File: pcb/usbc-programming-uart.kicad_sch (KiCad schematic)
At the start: 24 parts, among them J6 HC-TYPE-C-16P-01A, Q5 MMBT2222A, Q6 MMBT2222A, SW1 RST, SW2 BOOT, U10 AMS1117-3.3, U11 CH334R, U9 CH340C, Y1 12MHz

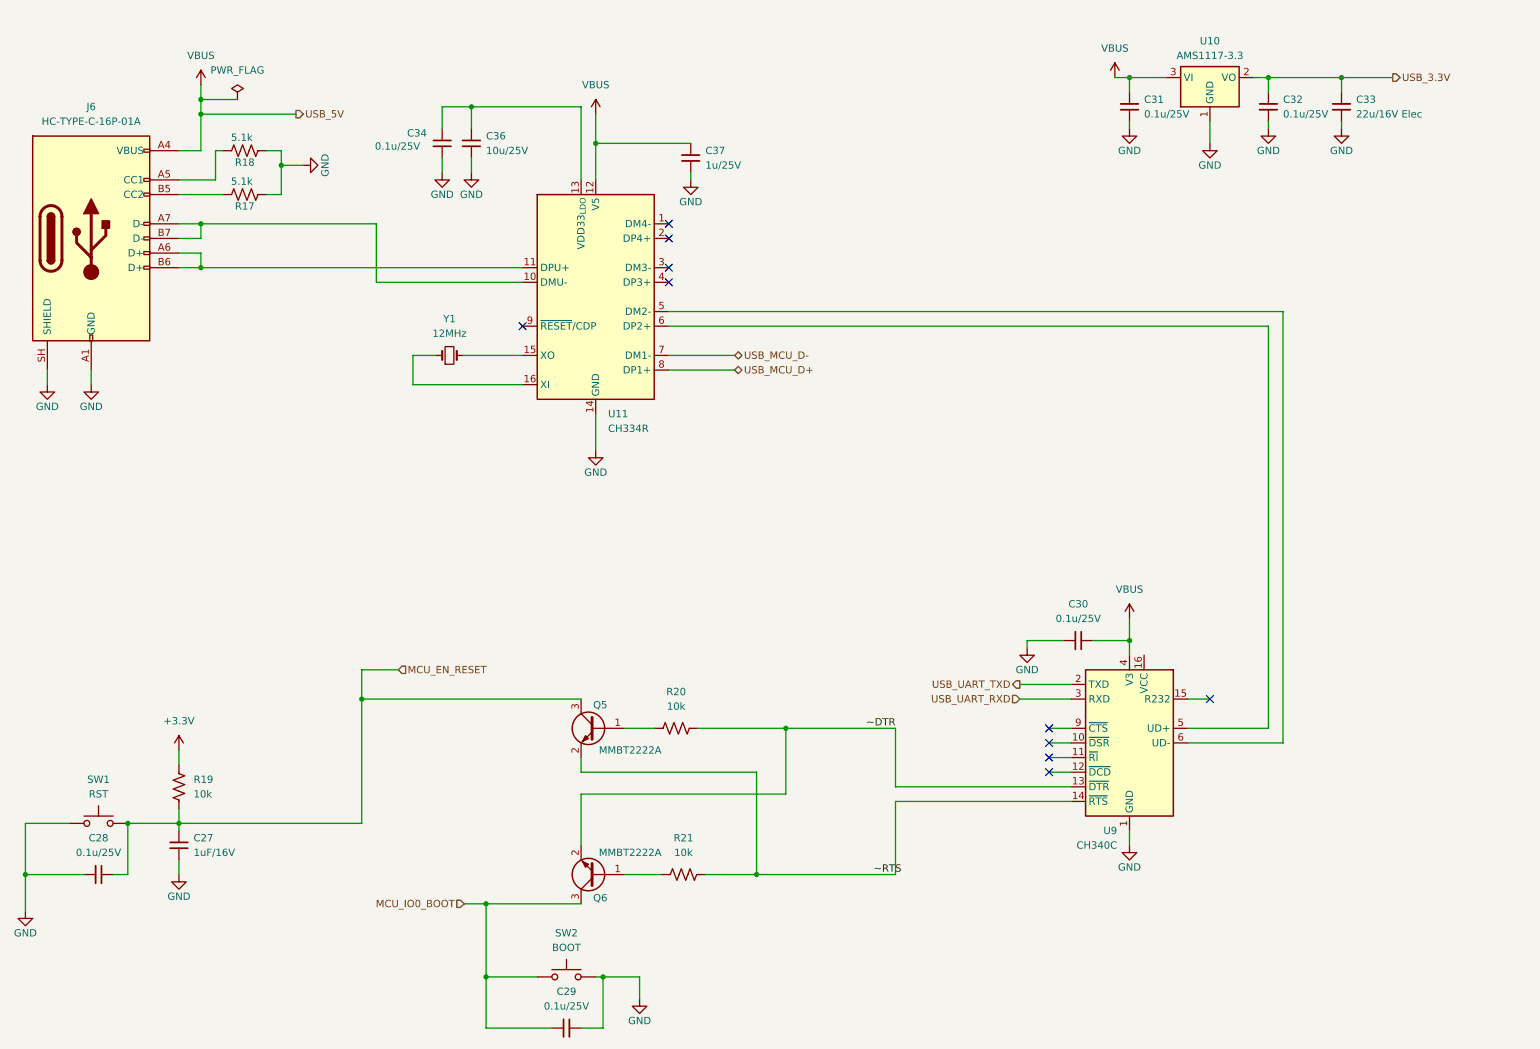
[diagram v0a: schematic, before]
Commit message: Replace battery/PowerPole ORing FETs with TPS2121 in VCOMP mode
power.kicad_sch: U12 (TPS2121RUXR) replaces the two LM74610+AO3400A ideal-
diode branches, configured per TI's "Highest Voltage Operation" (VCOMP,
Fig 10-15): PR1/CP2 tied to GND, OV1/OV2 resistor dividers (23.7k/5k) off
IN1 (PWR_18650) and IN2 (PWR_POWERPOLE), ILM set via R24 (51.1k), SS
ramped through C39 (0.01uF), ST tied directly to GND (unused). Divider
topology, ILM, and SS/ST wiring were each wrong on the first pass and
have been traced pin-by-pin and verified correct against the reference
schematic.

usbc-programming-uart.kicad_sch: CH340C VCC/V3 pin fix (VCC now correctly
powered from VBUS, V3 no longer driven externally) and F3 polyfuse
(16V/500mA) added in series on VBUS upstream of the hub/CH340/AMS1117.

battery_18650_input.kicad_sch, foxhunt1.kicad_pro: incidental KiCad
save cleanup (unused symbol-cache entry pruned, two collinear wire
segments merged, designator bookkeeping reordered) -- no circuit changes.

Bumps kicad_gx_library for the new TPS2121RUXR part. Adds
_docs/hardware/usb_battery_power_mux.md documenting the planned
3-stage TPS2121 architecture (this commit implements stage 1; stages
2/3, the USB-vs-regulator muxes, are not yet implemented).

Co-Authored-By: Claude Sonnet 5 <noreply@anthropic.com>
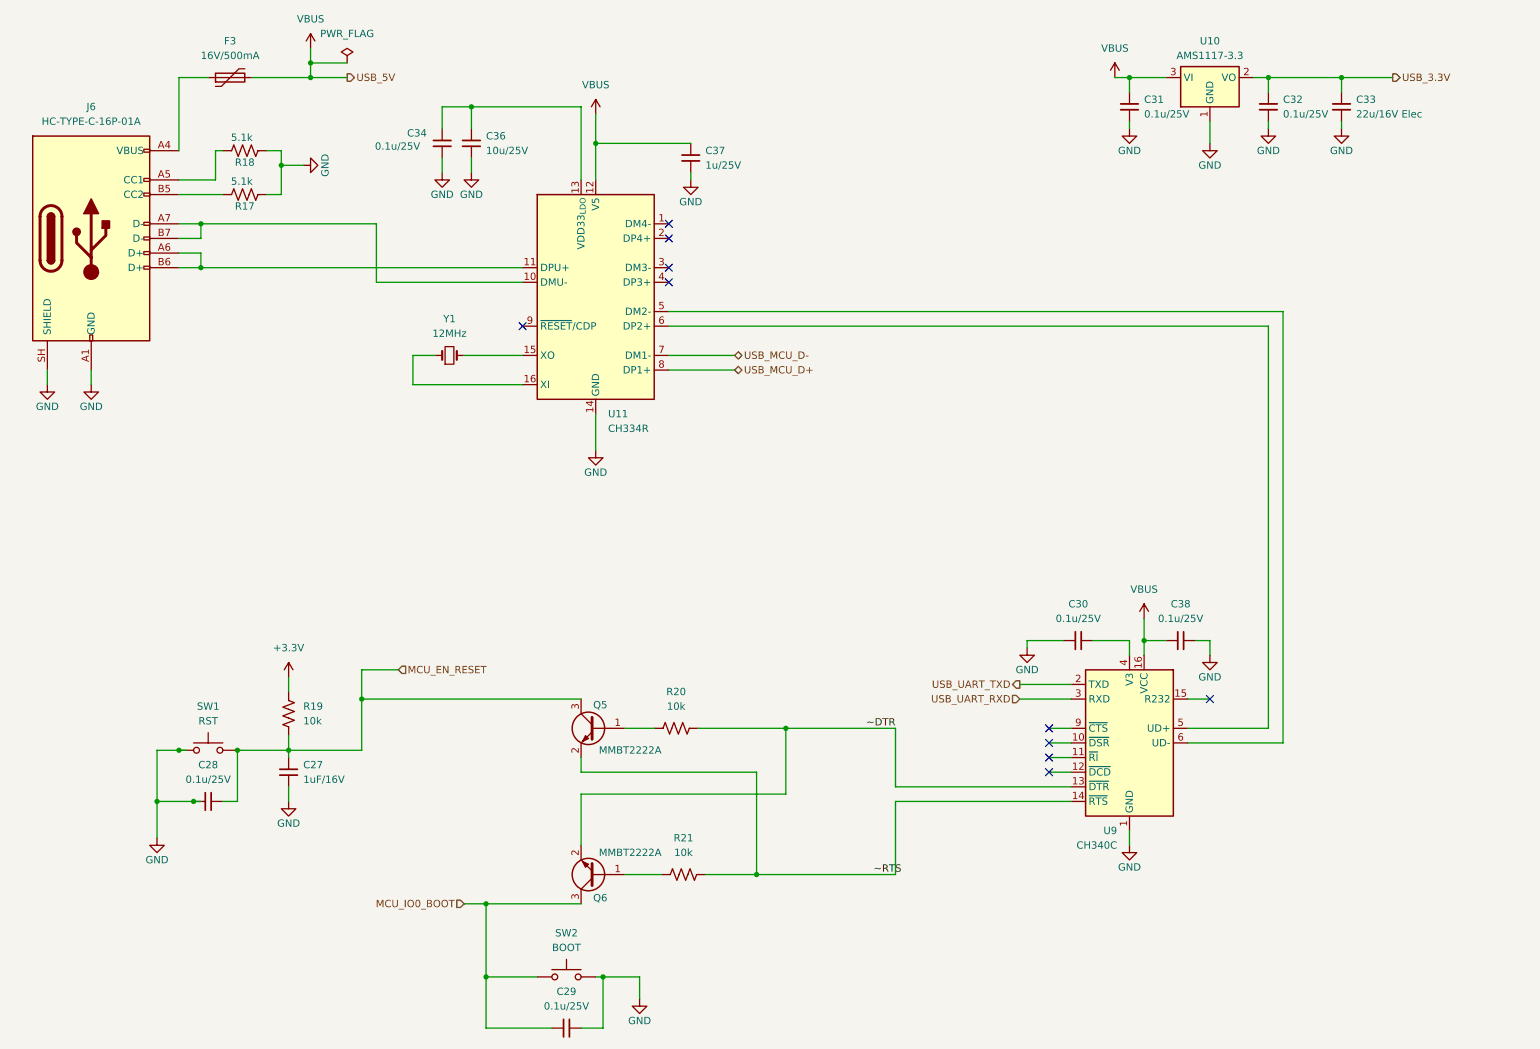
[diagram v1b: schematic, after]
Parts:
- added C38: 0.1u/25V, Capacitor_SMD:C_0603_1608Metric, symbol Device:C_Small
- added F3: 16V/500mA, Fuse:Fuse_0805_2012Metric, symbol Device:Polyfuse
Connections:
- net GND: now also C38.2
- net VBUS: now also U9.16 (VCC), C38.1, F3.2; no longer C30.2, J6.A4 (VBUS), J6.A9 (VBUS), J6.B4 (VBUS), J6.B9 (VBUS), U9.4 (V3)
- new net: F3.1, J6.A4 (VBUS), J6.A9 (VBUS), J6.B4 (VBUS), J6.B9 (VBUS)
- new net: C30.2, U9.4 (V3)
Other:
- moved on the sheet: C27, C28, R19, SW1

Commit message: Add TPS2121 Stage 2/3: USB-vs-battery priority muxing on 5V and 3.3V rails
power.kicad_sch:
- U14 (TPS2121RUXR): 5V rail mux. IN1=BATT_5V_REG (priority), IN2=USB_5V_IN,
  OUT=+5V. PR1 tied to IN1, CP2/OV1/OV2 to GND (VREF priority mode -- battery
  always wins when present, no voltage-comparison ambiguity between two
  nominally-5V sources). ILM set via R26 (30.1k, ~3.5A class, sized with
  margin above the 2A SA818 budget for TX current transients). SS via C42
  (0.01uF). ST feeds the battery/USB detect logic below.
- U13 (TPS2121RUXR): 3.3V rail mux, same configuration. IN1=BATT_3.3V_REG,
  IN2=USB_3.3V_IN, OUT=+3.3V. ILM via R25 (80.6k, ~1.5A class, vs 1A
  peripheral budget). SS via C41.
- U1 (74LVC1G08): AND-gates U13.ST and U14.ST (each pulled up individually
  via R27/R28, 10k to +3.3V, since ST is open-drain) into PWR_ON_BATTERY --
  high only when both rails are confirmed running from battery, low if
  either has fallen back to USB. Output exposed as a new Power sheet pin.

foxhunt1.kicad_sch: bridges PWR_ON_BATTERY (Power sheet) to the new
IO_IN_ON_BATT input on the mcu-esp32 sheet, and USB_3.3V_IN/USB_5V_IN
(Power sheet) to USB_3.3V/USB_5V (USB-C sheet) -- these were previously
unconnected placeholder labels.

mcu-esp32.kicad_sch: IO_IN_ON_BATT wired to U8 pin 35 (GPIO42), the one
GPIO the pinout doc had marked as still spare.

kicad_gx_library: TPS2121RUXR symbol fix (one OUT pin marked passive
instead of output, since the two physical OUT pins are meant to be tied
together -- avoids an ERC driver-conflict false positive).

power_regulation.kicad_sch, battery_18650_input.kicad_sch,
battery_powerpole_input.kicad_sch, foxhunt1.kicad_pro: incidental KiCad
save cleanup, no circuit changes (verified via orphan/short checks and
netlist diff -- same components as before).

Fully traced pin-by-pin: both mux dividers/ILM/SS wiring, the battery-vs-
USB source assignment on each rail (not swapped), the AND-gate inputs,
and all three cross-sheet bridges. 0 new orpha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
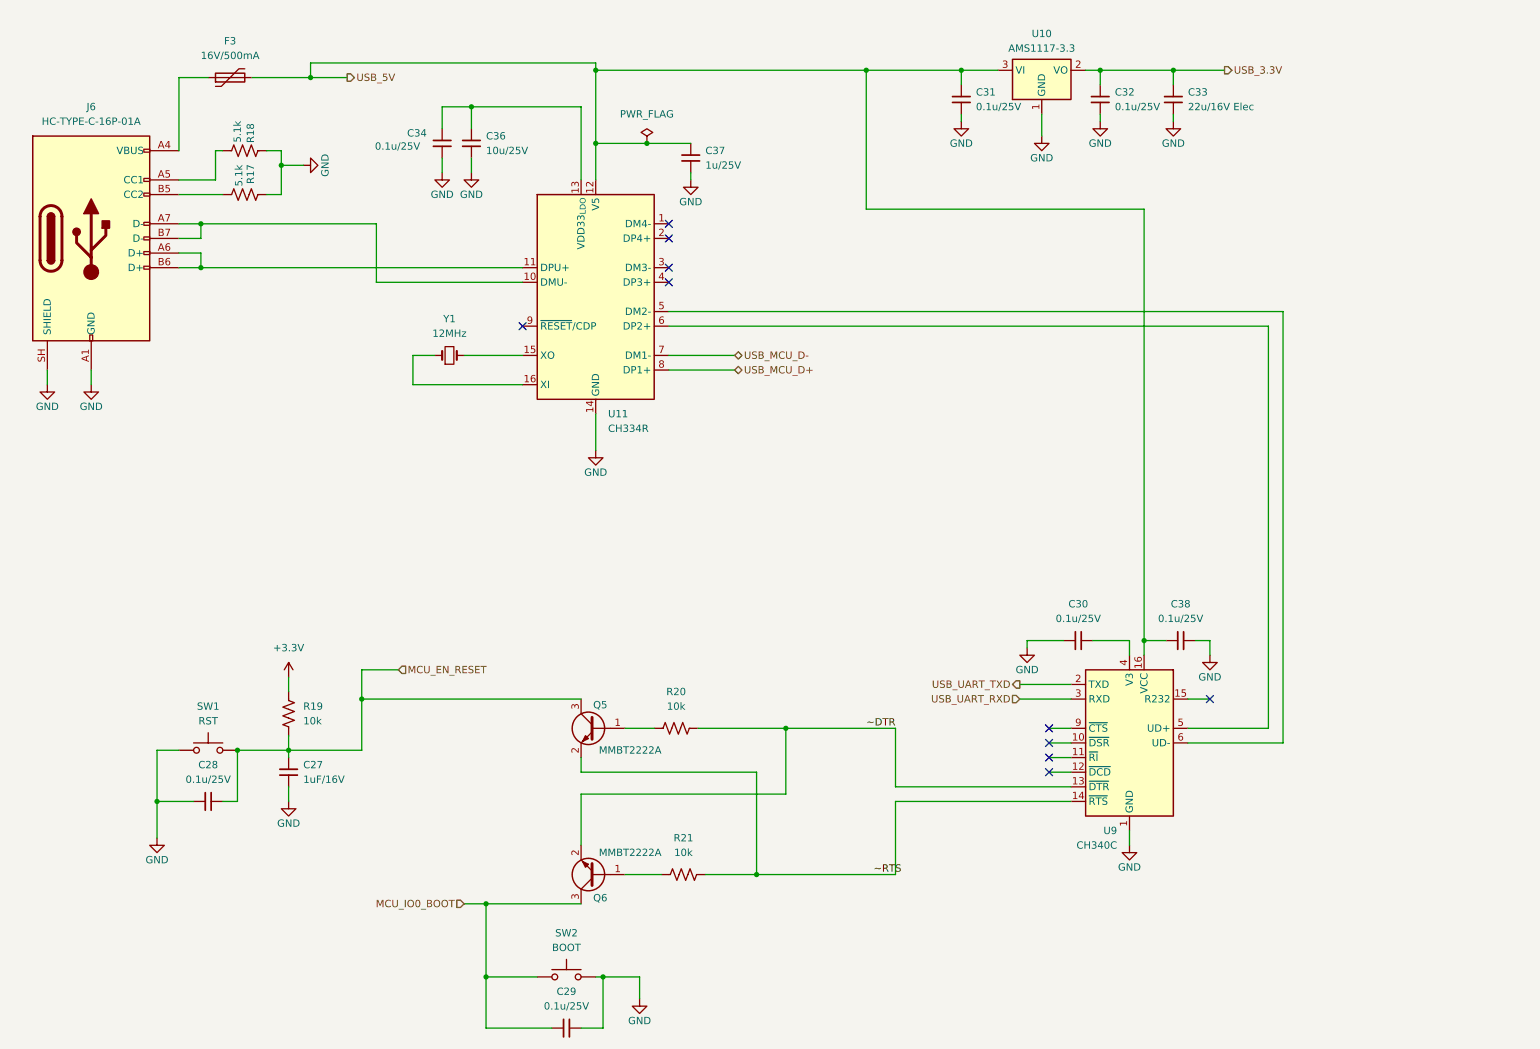
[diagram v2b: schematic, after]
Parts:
- R17, R18, R19, R20, R21: symbol PCM_SparkFun-Resistor:R -> Device:R_US
- SW1, SW2: footprint Button_Switch_SMD.pretty:SW_SPST_PTS645Sx43SMTR92 -> Button_Switch_SMD:SW_SPST_PTS645Sx43SMTR92
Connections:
- net +3.3V: now also R19.2; no longer R19.1
- net GND: now also R17.1, R18.1; no longer R17.2, R18.2
- net MCU_EN_RESET: now also R19.1; no longer R19.2
- net ~DTR: now also R20.1; no longer R20.2
- net ~RTS: now also R21.1; no longer R21.2
- net at J6.A5 (CC1): now also R18.2; no longer R18.1
- net at J6.B5 (CC2): now also R17.2; no longer R17.1
- net at Q6.1 (B): now also R21.2; no longer R21.1
- net at Q5.1 (B): now also R20.2; no longer R20.1
- net VBUS renamed USB_5V
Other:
- moved on the sheet: C31, C32, C33, R17, R18, R19, R20, R21, U10

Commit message: Full re-annotation, BOM audit fixes, Stage-1 ILM resize, and PCB reset
Schematic: re-annotated reference designators project-wide (3rd pass) --
every real component's designator has shifted since the last commit.
Fixed BOM gaps found by the fresh audit: U13 (CH340C) sourcing fields,
R7's Manf typo (YAGE -> YAGEO), R5/R8/R14 missing LCSC Part#s, and
normalized U1/U2/U3 (TPS2121RUXR) field names from easyeda2kicad's
defaults (Manufacturer/LCSC Part) to this project's convention
(Manf/LCSC Part #). Resized Stage 1's ILM resistor (R8) from 51.1k to
30.1k -- the prior value undersized the current limit for carrying both
downstream rails' combined battery-side current.

pcb/foxhunt1.kicad_pcb: cleared all footprints. No board layout has
started yet; this reflects that accurately rather than carrying stale
placements from before the schematic settled.

_agent_tasks/bom_property_audit.md: new reusable playbook for this BOM
audit (method, standing exceptions, reporting format), so future passes
don't have to re-derive the approach each time.

_docs/sourcing/task1_lcsc_crossreference.md: replaced stale results
(referencing pre-renumbering designators) with the current audit's
findings. One open item remains: the current-sense shunt's footprint
implies Vishay pad geometry but the sourced part is Milliohm-brand,
needs physical verification before fab.

Co-Authored-By: Claude Sonnet 5 <noreply@anthropic.com>
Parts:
- U13: renamed from U9; LCSC Part # (none) -> C84681; MPN (none) -> CH340C; Manf (none) -> WCH; Package (none) -> SOP-16
- renumbered C28 to C31, C27 to C32, C34 to C33, C36 to C34, C29 to C35, C37 to C36, C31 to C37, C30 to C38, C32 to C39, C33 to C40, C38 to C41, J6 to J3, Q5 to Q3, Q6 to Q4, R18 to R24, R17 to R25, R19 to R26, R20 to R27, R21 to R28, U10 to U12

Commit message: Add VRAW soft-latch power switch and MCU/RTC wake network
- Q5 (AO3407A P-FET) gates VRAW into Power Regulation, gate driven by
  a shared active-low wake node (button SW3, RTC_PWR_INTERRUPT,
  MCU_OUT_PWR_LATCH) pulled up to VRAW through 1M R29
- Q6 (BSS138) on the mcu-esp32 sheet lets GPIO48 hold the latch from
  a 3.3V-safe domain without exposing the MCU to VRAW voltage
- JP5/JP6 bench-isolation jumpers in the VRAW-gated path, bridged via
  new VRAW_GATED net label into Power Regulation's PWR_IN_SELECT
- JP24 lets USB be excluded from the TPS2121 power muxes for bench
  testing the sleep/wake cycle while still connected over USB-C
- Added blank Peripherals sheet (mcu-esp32 child) with RTC-facing
  pins stubbed and wired at the root, ready for the PCF8563 circuit
- regulation.md updated for the final 6.67V/4.78V intermediate
  voltages and matched-tolerance thin-film feedback dividers
- open_items.md: added power-off path as a follow-up (latch only
  handles power-on today)

Co-Authored-By: Claude Sonnet 5 <noreply@anthropic.com>
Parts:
- added JP24: Jumper_2_Open, TestPoint:TestPoint_2Pads_Pitch2.54mm_Drill0.8mm, symbol Jumper:Jumper_2_Open
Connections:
- net USB_5V: now also JP24.2 (B); no longer C36.1, C41.1, F3.2, U11.12 (V5), U13.16 (VCC)
- new net: C36.1, C41.1, F3.2, JP24.1 (A), U11.12 (V5), U13.16 (VCC)
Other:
- moved on the sheet: C37, C39, C40, U12

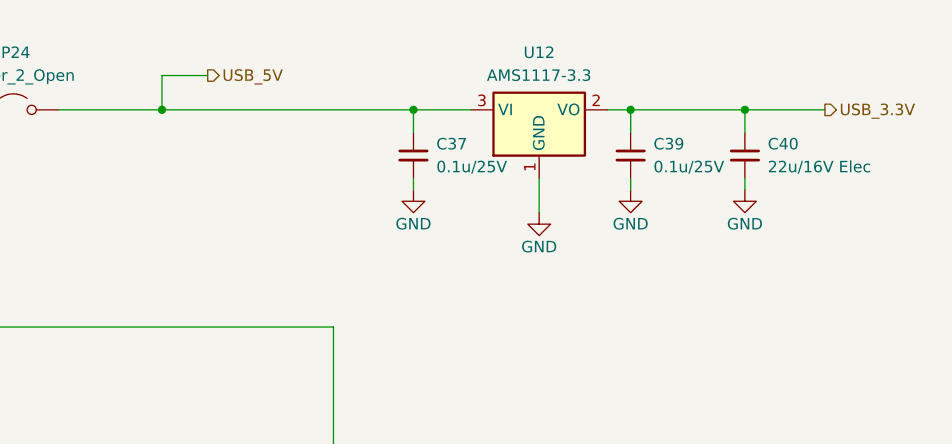
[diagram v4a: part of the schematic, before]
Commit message: Wire up PCA9555 expansion IO section, source LEDs/resistors, swap 3.3V LDO to LM1117
- PCA9555PW expansion IO: DIP switch (SW4, IO0_0-3), onboard buttons
  (SW7-10), status LEDs (D7-10) with sourced series resistors, external
  JST breakouts (J4-7/R39-42) for IO0_4-7, INT pull-up (R34), VDD bypass
  (C49), address pins grounded (addr 0x20)
- Route PCA9555 INT (PERIPH_IO_INT) across the Power/mcu-esp32 top-level
  sheets to the ESP32-S3 (MCU_IN_IO_INT)
- Source real YAGEO MPN/LCSC part numbers for R30/R31/R34-R42
- Fix D10 LED (was orange 0603 with an LCSC part# that resolved to a
  different, wrong part) -> yellow 0805 APTD2012LSYCK, verified Vf/LCSC
  match, matching D7-9's package family
- Fix stale copy-pasted Datasheet links on D7-9 and R31/R35
- Swap 3.3V LDO from AMS1117-3.3 to TI LM1117IMPX-3.3/NOPB (5V LDO swap
  from LM1085IS-5.0 still pending)

Co-Authored-By: Claude Sonnet 5 <noreply@anthropic.com>
Claude-Session: https://claude.ai/code/session_01LhLkuH6sQ5GbUZ61bG7p2h
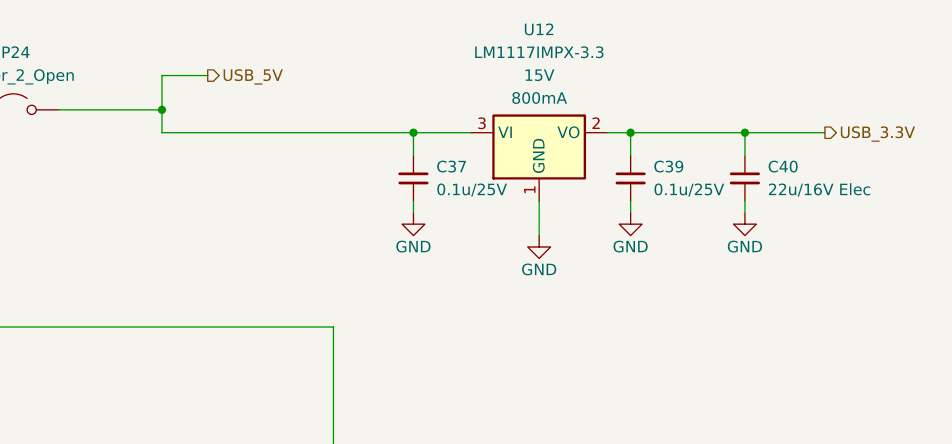
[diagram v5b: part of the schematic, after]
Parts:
- removed U12: AMS1117-3.3, Package_TO_SOT_SMD:SOT-223-3_TabPin2, symbol Regulator_Linear:AMS1117-3.3
- added U12: LM1117IMPX-3.3, Package_TO_SOT_SMD:SOT-223, symbol PCM_SparkFun-Regulator:LM1117-3.3
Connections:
- net GND: now also U12.1 (GND)
- net USB_3.3V: now also U12.2 (VO)
- net USB_5V: now also U12.3 (VI)
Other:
- moved on the sheet: C37, C39, C40
